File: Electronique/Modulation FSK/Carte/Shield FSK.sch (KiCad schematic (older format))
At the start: 11 parts

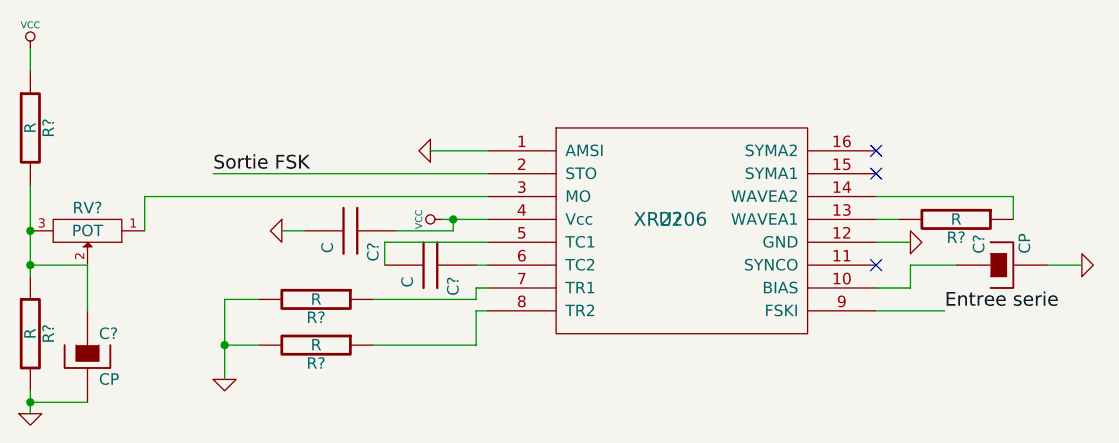
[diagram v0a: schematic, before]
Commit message: On commence l'association enpreintes pour le shield FSK
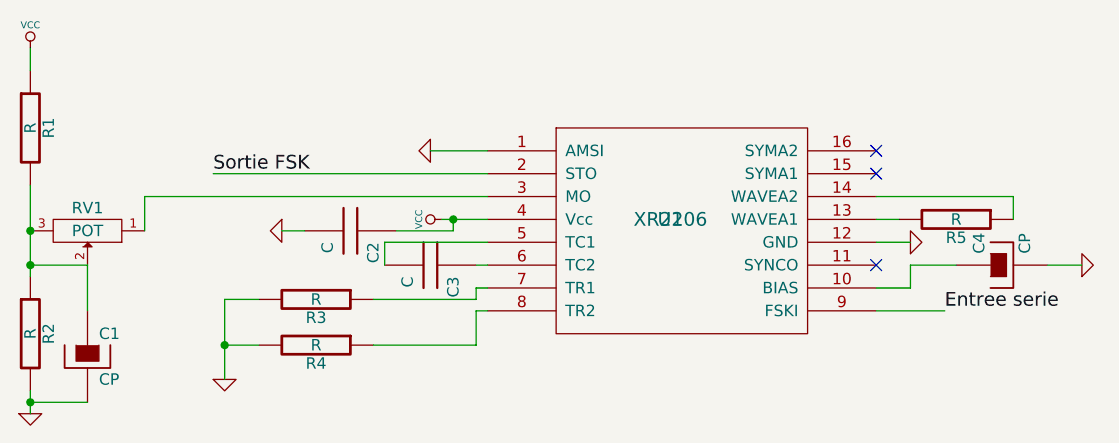
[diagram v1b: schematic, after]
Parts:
- gave numbers to parts that had none: 11
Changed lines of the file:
@@
-EESchema Schematic File Version 2  date 10/03/2012 17:59:58
+EESchema Schematic File Version 2  date 10/03/2012 18:50:52
 LIBS:power
 LIBS:device
@@
 $EndDescr
 $Comp
-L CP C?
+L CP C4
 U 1 1 4F5B8873
 P 6850 4000
-F 0 "C?" H 6900 4100 50  0000 L CNN
+F 0 "C4" H 6900 4100 50  0000 L CNN
 F 1 "CP" H 6900 3900 50  0000 L CNN
 	1    6850 4000
@@
 	2850 4000 2850 4200
 $Comp
-L CP C?
+L CP C1
 U 1 1 4F5B87DA
 P 2850 4400
-F 0 "C?" H 2900 4500 50  0000 L CNN
+F 0 "C1" H 2900 4500 50  0000 L CNN
 F 1 "CP" H 2900 4300 50  0000 L CNN
 	1    2850 4400
@@
 $EndComp
 $Comp
-L GND #PWR?
+L GND #PWR01
 U 1 1 4F5B8724
 P 2600 4650
-F 0 "#PWR?" H 2600 4650 30  0001 C CNN
+F 0 "#PWR01" H 2600 4650 30  0001 C CNN
 F 1 "GND" H 2600 4580 30  0001 C CNN
 	1    2600 4650
@@
 $EndComp
 $Comp
-L VCC #PWR?
+L VCC #PWR02
 U 1 1 4F5B8719
 P 2600 3050
-F 0 "#PWR?" H 2600 3150 30  0001 C CNN
+F 0 "#PWR02" H 2600 3150 30  0001 C CNN
 F 1 "VCC" H 2600 3150 30  0000 C CNN
 	1    2600 3050
@@
 $EndComp
 $Comp
-L R R?
+L R R2
 U 1 1 4F5B870F
 P 2600 4300
-F 0 "R?" V 2680 4300 50  0000 C CNN
+F 0 "R2" V 2680 4300 50  0000 C CNN
 F 1 "R" V 2600 4300 50  0000 C CNN
 	1    2600 4300
@@
 $EndComp
 $Comp
-L R R?
+L R R1
 U 1 1 4F5B8708
 P 2600 3400
-F 0 "R?" V 2680 3400 50  0000 C CNN
+F 0 "R1" V 2680 3400 50  0000 C CNN
 F 1 "R" V 2600 3400 50  0000 C CNN
 	1    2600 3400
@@
 $EndComp
 $Comp
-L POT RV?
+L POT RV1
 U 1 1 4F5B867D
 P 2850 3850
-F 0 "RV?" H 2850 3750 50  0000 C CNN
+F 0 "RV1" H 2850 3750 50  0000 C CNN
 F 1 "POT" H 2850 3850 50  0000 C CNN
 	1    2850 3850
@@
 NoConn ~ 6300 3600
 $Comp
-L R R?
+L R R5
 U 1 1 4F5B7612
 P 6650 3800
-F 0 "R?" V 6730 3800 50  0000 C CNN
+F 0 "R5" V 6730 3800 50  0000 C CNN
 F 1 "R" V 6650 3800 50  0000 C CNN
 	1    6650 3800
@@
 $EndComp
 $Comp
-L GND #PWR?
+L GND #PWR03
 U 1 1 4F5B75FB
 P 7200 4000
-F 0 "#PWR?" H 7200 4000 30  0001 C CNN
+F 0 "#PWR03" H 7200 4000 30  0001 C CNN
 F 1 "GND" H 7200 3930 30  0001 C CNN
 	1    7200 4000
@@
 Entree serie
 $Comp
-L GND #PWR?
+L GND #PWR04
 U 1 1 4F5B733F
 P 3450 4500
-F 0 "#PWR?" H 3450 4500 30  0001 C CNN
+F 0 "#PWR04" H 3450 4500 30  0001 C CNN
 F 1 "GND" H 3450 4430 30  0001 C CNN
 	1    3450 4500
@@
 $EndComp
 $Comp
-L R R?
+L R R4
 U 1 1 4F5B7320
 P 3850 4350
-F 0 "R?" V 3930 4350 50  0000 C CNN
+F 0 "R4" V 3930 4350 50  0000 C CNN
 F 1 "R" V 3850 4350 50  0000 C CNN
 	1    3850 4350
@@
 $EndComp
 $Comp
-L R R?
+L R R3
 U 1 1 4F5B7305
 P 3850 4150
-F 0 "R?" V 3930 4150 50  0000 C CNN
+F 0 "R3" V 3930 4150 50  0000 C CNN
 F 1 "R" V 3850 4150 50  0000 C CNN
 	1    3850 4150
@@
 Sortie FSK
 $Comp
-L C C?
+L C C3
 U 1 1 4F5B723C
 P 4350 4000
-F 0 "C?" H 4400 4100 50  0000 L CNN
+F 0 "C3" H 4400 4100 50  0000 L CNN
 F 1 "C" H 4400 3900 50  0000 L CNN
 	1    4350 4000
@@
 $EndComp
 $Comp
-L GND #PWR?
+L GND #PWR05
 U 1 1 4F5B7223
 P 3700 3850
-F 0 "#PWR?" H 3700 3850 30  0001 C CNN
+F 0 "#PWR05" H 3700 3850 30  0001 C CNN
 F 1 "GND" H 3700 3780 30  0001 C CNN
 	1    3700 3850
@@
 $EndComp
 $Comp
-L C C?
+L C C2
 U 1 1 4F5B720F
 P 4000 3850
-F 0 "C?" H 4050 3950 50  0000 L CNN
+F 0 "C2" H 4050 3950 50  0000 L CNN
 F 1 "C" H 4050 3750 50  0000 L CNN
 	1    4000 3850
@@
 $EndComp
 $Comp
-L GND #PWR?
+L GND #PWR06
 U 1 1 4F5B70E7
 P 4350 3500
-F 0 "#PWR?" H 4350 3500 30  0001 C CNN
+F 0 "#PWR06" H 4350 3500 30  0001 C CNN
 F 1 "GND" H 4350 3430 30  0001 C CNN
 	1    4350 3500
@@
 $EndComp
 $Comp
-L GND #PWR?
+L GND #PWR07
 U 1 1 4F5B7069
 P 6450 3900
-F 0 "#PWR?" H 6450 3900 30  0001 C CNN
+F 0 "#PWR07" H 6450 3900 30  0001 C CNN
 F 1 "GND" H 6450 3830 30  0001 C CNN
 	1    6450 3900
@@
 $EndComp
 $Comp
-L VCC #PWR?
+L VCC #PWR08
 U 1 1 4F5B7056
 P 4400 3800
-F 0 "#PWR?" H 4400 3900 30  0001 C CNN
+F 0 "#PWR08" H 4400 3900 30  0001 C CNN
 F 1 "VCC" H 4400 3900 30  0000 C CNN
 	1    4400 3800
@@
 $EndComp
 $Comp
-L XR2206 U?
+L XR2206 U1
 U 1 1 4F5B704A
 P 5400 3800
-F 0 "U?" H 5400 3800 60  0000 C CNN
+F 0 "U1" H 5400 3800 60  0000 C CNN
 F 1 "XR2206" H 5400 3800 60  0000 C CNN
 	1    5400 3800

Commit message: Carte FSK routée !!!
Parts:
- added SHIELD1: ARDUINO_SHIELD, symbol ARDUINO_SHIELD
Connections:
- net Entree serie: now also SHIELD1.1
- net GND: now also SHIELD1.GND1
- new net +5V: SHIELD1.5V
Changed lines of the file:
@@
-EESchema Schematic File Version 2  date 10/03/2012 18:50:52
+EESchema Schematic File Version 2  date 22/03/2012 21:51:35
 LIBS:power
 LIBS:device
@@
 LIBS:contrib
 LIBS:valves
+LIBS:Arduino
+LIBS:arduino_shieldsNCL
 LIBS:Shield FSK-cache
 EELAYER 25  0
@@
 Sheet 1 1
 Title ""
-Date "10 mar 2012"
+Date "22 mar 2012"
 Rev ""
 Comp ""
@@
 Comment4 ""
 $EndDescr
+Text Label 6500 3000 0    60   ~ 0
+Entree serie
+Wire Wire Line
+	6400 3000 6500 3000
+Wire Wire Line
+	4400 2100 4500 2100
+Wire Wire Line
+	2850 4200 2850 4000
+Wire Wire Line
+	2600 4550 2600 4650
+Wire Wire Line
+	2600 3650 2600 4050
+Connection ~ 2600 3850
+Wire Wire Line
+	3100 3850 3100 3700
+Wire Wire Line
+	3100 3700 4600 3700
+Wire Wire Line
+	6300 3800 6400 3800
+Wire Wire Line
+	6650 4000 6450 4000
+Wire Wire Line
+	6450 4000 6450 4100
+Wire Wire Line
+	6450 4100 6300 4100
+Connection ~ 3450 4350
+Wire Wire Line
+	3600 4350 3450 4350
+Wire Wire Line
+	4100 4350 4550 4350
+Wire Wire Line
+	4550 4350 4550 4200
+Wire Wire Line
+	4550 4200 4600 4200
+Wire Wire Line
+	4100 4150 4550 4150
+Wire Wire Line
+	4550 4150 4550 4100
+Wire Wire Line
+	4550 4100 4600 4100
+Wire Wire Line
+	4600 4000 4550 4000
+Wire Wire Line
+	4200 3850 4450 3850
+Connection ~ 4450 3800
+Wire Wire Line
+	4450 3850 4450 3800
+Wire Wire Line
+	6450 3900 6300 3900
+Wire Wire Line
+	4400 3800 4600 3800
+Wire Wire Line
+	4600 3500 4350 3500
+Wire Wire Line
+	3400 3600 4600 3600
+Wire Wire Line
+	3800 3850 3700 3850
+Wire Wire Line
+	4600 3900 4150 3900
+Wire Wire Line
+	4150 3900 4150 4000
+Wire Wire Line
+	3600 4150 3450 4150
+Wire Wire Line
+	3450 4150 3450 4500
+Wire Wire Line
+	6600 4200 6300 4200
+Wire Wire Line
+	7050 4000 7200 4000
+Wire Wire Line
+	6900 3800 6900 3700
+Wire Wire Line
+	6900 3700 6300 3700
+Wire Wire Line
+	2850 4000 2600 4000
+Connection ~ 2600 4000
+Wire Wire Line
+	2600 3050 2600 3150
+Wire Wire Line
+	2850 4600 2600 4600
+Connection ~ 2600 4600
+Wire Wire Line
+	4500 2200 4400 2200
+Text GLabel 3400 3600 0    60   Input ~ 0
+Sortie FSK
+$Comp
+L GND #PWR01
+U 1 1 4F6B897D
+P 4400 2200
+F 0 "#PWR01" H 4400 2200 30  0001 C CNN
+F 1 "GND" H 4400 2130 30  0001 C CNN
+	1    4400 2200
+	0    1    1    0
+$EndComp
+$Comp
+L +5V #PWR02
+U 1 1 4F6B8971
+P 4400 2100
+F 0 "#PWR02" H 4400 2190 20  0001 C CNN
+F 1 "+5V" H 4400 2190 30  0000 C CNN
+	1    4400 2100
+	0    -1   -1   0
+$EndComp
+$Comp
+L ARDUINO_SHIELD SHIELD1
+U 1 1 4F6B8878
+P 5450 2300
+F 0 "SHIELD1" H 5100 3250 60  0000 C CNN
+F 1 "ARDUINO_SHIELD" H 5500 1350 60  0000 C CNN
+	1    5450 2300
+	1    0    0    -1
+$EndComp
 $Comp
 L CP C4
@@
 	0    -1   -1   0
 $EndComp
-Connection ~ 2600 4600
-Wire Wire Line
-	2850 4600 2600 4600
-Wire Wire Line
-	2600 3050 2600 3150
-Connection ~ 2600 4000
-Wire Wire Line
-	2600 4000 2850 4000
-Wire Wire Line
-	6300 3700 6900 3700
-Wire Wire Line
-	6900 3700 6900 3800
-Wire Wire Line
-	7050 4000 7200 4000
-Wire Wire Line
-	6600 4200 6300 4200
-Wire Wire Line
-	3450 4500 3450 4150
-Wire Wire Line
-	3450 4150 3600 4150
-Wire Wire Line
-	4150 4000 4150 3900
-Wire Wire Line
-	4150 3900 4600 3900
-Wire Wire Line
-	3800 3850 3700 3850
-Wire Wire Line
-	3400 3600 4600 3600
-Wire Wire Line
-	4600 3500 4350 3500
-Wire Wire Line
-	4400 3800 4600 3800
-Wire Wire Line
-	6450 3900 6300 3900
-Wire Wire Line
-	4450 3800 4450 3850
-Connection ~ 4450 3800
-Wire Wire Line
-	4450 3850 4200 3850
-Wire Wire Line
-	4600 4000 4550 4000
-Wire Wire Line
-	4600 4100 4550 4100
-Wire Wire Line
-	4550 4100 4550 4150
-Wire Wire Line
-	4550 4150 4100 4150
-Wire Wire Line
-	4600 4200 4550 4200
-Wire Wire Line
-	4550 4200 4550 4350
-Wire Wire Line
-	4550 4350 4100 4350
-Wire Wire Line
-	3600 4350 3450 4350
-Connection ~ 3450 4350
-Wire Wire Line
-	6300 4100 6450 4100
-Wire Wire Line
-	6450 4100 6450 4000
-Wire Wire Line
-	6450 4000 6650 4000
-Wire Wire Line
-	6300 3800 6400 3800
-Wire Wire Line
-	4600 3700 3100 3700
-Wire Wire Line
-	3100 3700 3100 3850
-Connection ~ 2600 3850
-Wire Wire Line
-	2600 3650 2600 4050
-Wire Wire Line
-	2600 4550 2600 4650
-Wire Wire Line
-	2850 4000 2850 4200
 $Comp
 L CP C1
@@
 $EndComp
 $Comp
-L GND #PWR01
+L GND #PWR03
 U 1 1 4F5B8724
 P 2600 4650
-F 0 "#PWR01" H 2600 4650 30  0001 C CNN
+F 0 "#PWR03" H 2600 4650 30  0001 C CNN
 F 1 "GND" H 2600 4580 30  0001 C CNN
 	1    2600 4650
@@
 $EndComp
 $Comp
-L VCC #PWR02
+L VCC #PWR04
 U 1 1 4F5B8719
 P 2600 3050
-F 0 "#PWR02" H 2600 3150 30  0001 C CNN
+F 0 "#PWR04" H 2600 3150 30  0001 C CNN
 F 1 "VCC" H 2600 3150 30  0000 C CNN
 	1    2600 3050
@@
 $EndComp
 $Comp
-L GND #PWR03
+L GND #PWR05
 U 1 1 4F5B75FB
 P 7200 4000
-F 0 "#PWR03" H 7200 4000 30  0001 C CNN
+F 0 "#PWR05" H 7200 4000 30  0001 C CNN
 F 1 "GND" H 7200 3930 30  0001 C CNN
 	1    7200 4000
@@
 Entree serie
 $Comp
-L GND #PWR04
+L GND #PWR06
 U 1 1 4F5B733F
 P 3450 4500
-F 0 "#PWR04" H 3450 4500 30  0001 C CNN
+F 0 "#PWR06" H 3450 4500 30  0001 C CNN
 F 1 "GND" H 3450 4430 30  0001 C CNN
 	1    3450 4500
@@
 	0    1    1    0
 $EndComp
-Text Label 3400 3600 0    60   ~ 0
-Sortie FSK
 $Comp
 L C C3
@@
 $EndComp
 $Comp
-L GND #PWR05
+L GND #PWR07
 U 1 1 4F5B7223
 P 3700 3850
-F 0 "#PWR05" H 3700 3850 30  0001 C CNN
+F 0 "#PWR07" H 3700 3850 30  0001 C CNN
 F 1 "GND" H 3700 3780 30  0001 C CNN
 	1    3700 3850
@@
 $EndComp
 $Comp
-L GND #PWR06
+L GND #PWR08
 U 1 1 4F5B70E7
 P 4350 3500
-F 0 "#PWR06" H 4350 3500 30  0001 C CNN
+F 0 "#PWR08" H 4350 3500 30  0001 C CNN
 F 1 "GND" H 4350 3430 30  0001 C CNN
 	1    4350 3500
@@
 $EndComp
 $Comp
-L GND #PWR07
+L GND #PWR09
 U 1 1 4F5B7069
 P 6450 3900
-F 0 "#PWR07" H 6450 3900 30  0001 C CNN
+F 0 "#PWR09" H 6450 3900 30  0001 C CNN
 F 1 "GND" H 6450 3830 30  0001 C CNN
 	1    6450 3900
@@
 $EndComp
 $Comp
-L VCC #PWR08
+L VCC #PWR010
 U 1 1 4F5B7056
 P 4400 3800
-F 0 "#PWR08" H 4400 3900 30  0001 C CNN
+F 0 "#PWR010" H 4400 3900 30  0001 C CNN
 F 1 "VCC" H 4400 3900 30  0000 C CNN
 	1    4400 3800

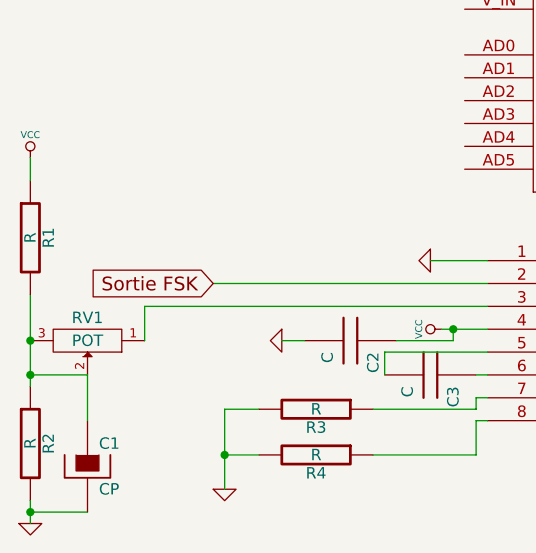
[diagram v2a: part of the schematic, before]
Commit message: On améliore un peu le routage
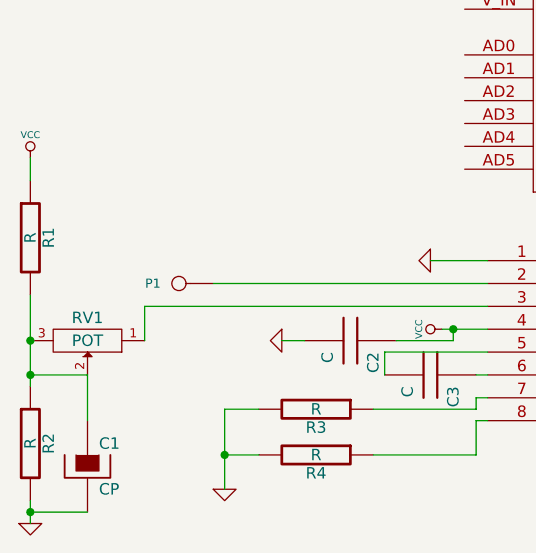
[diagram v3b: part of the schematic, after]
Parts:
- added P1: CONN_1, symbol CONN_1
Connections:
- net Sortie FSK: no longer names the net of U1.2 (STO)
- net Sortie FSK: now also P1.1
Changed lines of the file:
@@
-EESchema Schematic File Version 2  date 22/03/2012 21:51:35
+EESchema Schematic File Version 2  date 23/03/2012 16:19:35
 LIBS:power
 LIBS:device
@@
 Sheet 1 1
 Title ""
-Date "22 mar 2012"
+Date "23 mar 2012"
 Rev ""
 Comp ""
@@
 Comment4 ""
 $EndDescr
+$Comp
+L CONN_1 P1
+U 1 1 4F6C926A
+P 3250 3600
+F 0 "P1" H 3330 3600 40  0000 L CNN
+F 1 "CONN_1" H 3250 3655 30  0001 C CNN
+	1    3250 3600
+	-1   0    0    1
+$EndComp
 Text Label 6500 3000 0    60   ~ 0
 Entree serie
@@
 Wire Wire Line
 	4500 2200 4400 2200
-Text GLabel 3400 3600 0    60   Input ~ 0
-Sortie FSK
-$Comp
-L GND #PWR01
+$Comp
+L GND #PWR7
 U 1 1 4F6B897D
 P 4400 2200
-F 0 "#PWR01" H 4400 2200 30  0001 C CNN
+F 0 "#PWR7" H 4400 2200 30  0001 C CNN
 F 1 "GND" H 4400 2130 30  0001 C CNN
 	1    4400 2200
@@
 $EndComp
 $Comp
-L +5V #PWR02
+L +5V #PWR6
 U 1 1 4F6B8971
 P 4400 2100
-F 0 "#PWR02" H 4400 2190 20  0001 C CNN
+F 0 "#PWR6" H 4400 2190 20  0001 C CNN
 F 1 "+5V" H 4400 2190 30  0000 C CNN
 	1    4400 2100
@@
 $EndComp
 $Comp
-L GND #PWR03
+L GND #PWR2
 U 1 1 4F5B8724
 P 2600 4650
-F 0 "#PWR03" H 2600 4650 30  0001 C CNN
+F 0 "#PWR2" H 2600 4650 30  0001 C CNN
 F 1 "GND" H 2600 4580 30  0001 C CNN
 	1    2600 4650
@@
 $EndComp
 $Comp
-L VCC #PWR04
+L VCC #PWR1
 U 1 1 4F5B8719
 P 2600 3050
-F 0 "#PWR04" H 2600 3150 30  0001 C CNN
+F 0 "#PWR1" H 2600 3150 30  0001 C CNN
 F 1 "VCC" H 2600 3150 30  0000 C CNN
 	1    2600 3050
@@
 $EndComp
 $Comp
-L GND #PWR05
+L GND #PWR10
 U 1 1 4F5B75FB
 P 7200 4000
-F 0 "#PWR05" H 7200 4000 30  0001 C CNN
+F 0 "#PWR10" H 7200 4000 30  0001 C CNN
 F 1 "GND" H 7200 3930 30  0001 C CNN
 	1    7200 4000
@@
 Entree serie
 $Comp
-L GND #PWR06
+L GND #PWR3
 U 1 1 4F5B733F
 P 3450 4500
-F 0 "#PWR06" H 3450 4500 30  0001 C CNN
+F 0 "#PWR3" H 3450 4500 30  0001 C CNN
 F 1 "GND" H 3450 4430 30  0001 C CNN
 	1    3450 4500
@@
 $EndComp
 $Comp
-L GND #PWR07
+L GND #PWR4
 U 1 1 4F5B7223
 P 3700 3850
-F 0 "#PWR07" H 3700 3850 30  0001 C CNN
+F 0 "#PWR4" H 3700 3850 30  0001 C CNN
 F 1 "GND" H 3700 3780 30  0001 C CNN
 	1    3700 3850
@@
 $EndComp
 $Comp
-L GND #PWR08
+L GND #PWR5
 U 1 1 4F5B70E7
 P 4350 3500
-F 0 "#PWR08" H 4350 3500 30  0001 C CNN
+F 0 "#PWR5" H 4350 3500 30  0001 C CNN
 F 1 "GND" H 4350 3430 30  0001 C CNN
 	1    4350 3500
@@
 $EndComp
 $Comp
-L GND #PWR09
+L GND #PWR9
 U 1 1 4F5B7069
 P 6450 3900
-F 0 "#PWR09" H 6450 3900 30  0001 C CNN
+F 0 "#PWR9" H 6450 3900 30  0001 C CNN
 F 1 "GND" H 6450 3830 30  0001 C CNN
 	1    6450 3900
@@
 $EndComp
 $Comp
-L VCC #PWR010
+L VCC #PWR8
 U 1 1 4F5B7056
 P 4400 3800
-F 0 "#PWR010" H 4400 3900 30  0001 C CNN
+F 0 "#PWR8" H 4400 3900 30  0001 C CNN
 F 1 "VCC" H 4400 3900 30  0000 C CNN
 	1    4400 3800
